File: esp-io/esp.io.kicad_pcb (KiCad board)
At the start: 2 copper layers, 91.9 x 86 mm, 76 parts, among them P1 CONN_2, P2 CONN_01X02, P3 CONN_01X02, P4 CONN_01X02, P5 CONN_01X02, Q1 NPN, Q2 NPN, Q3 NPN, Q4 NPN, Q5 NPN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

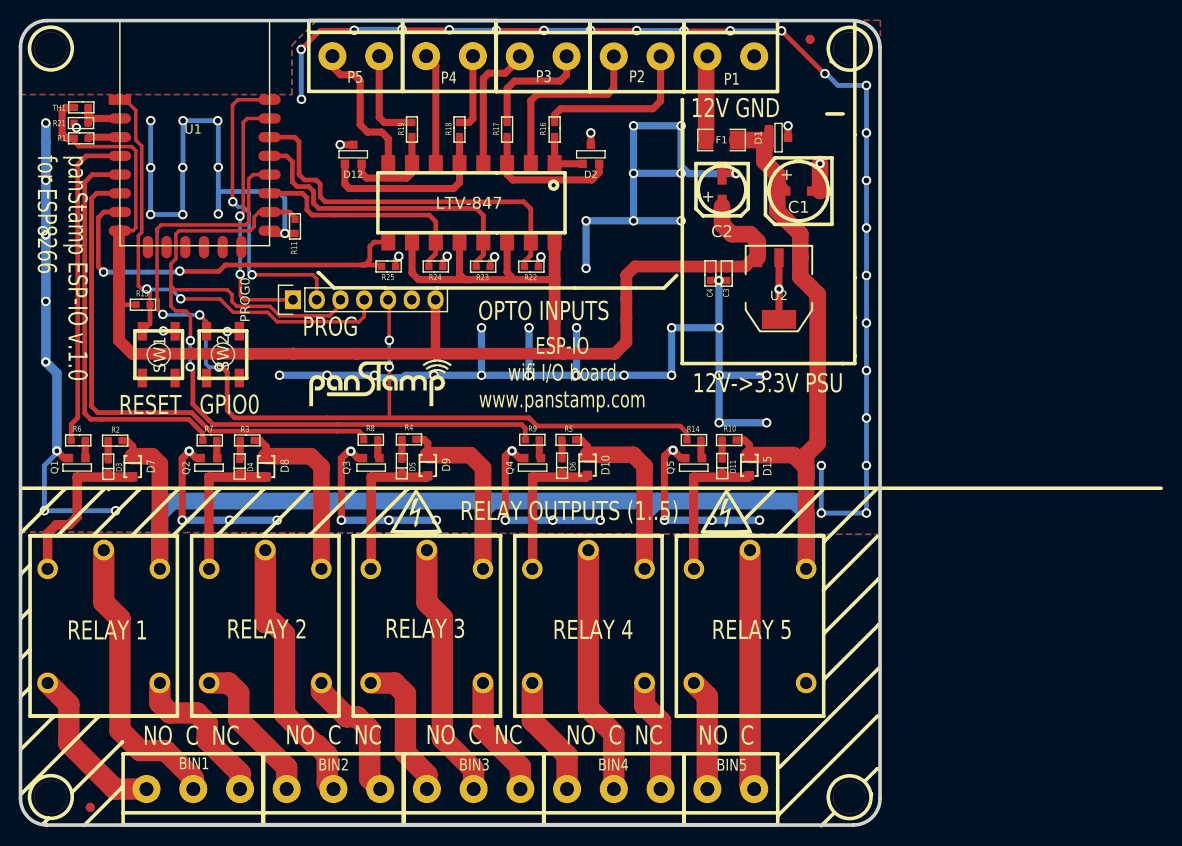
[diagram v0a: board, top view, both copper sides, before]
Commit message: fifth relay removed
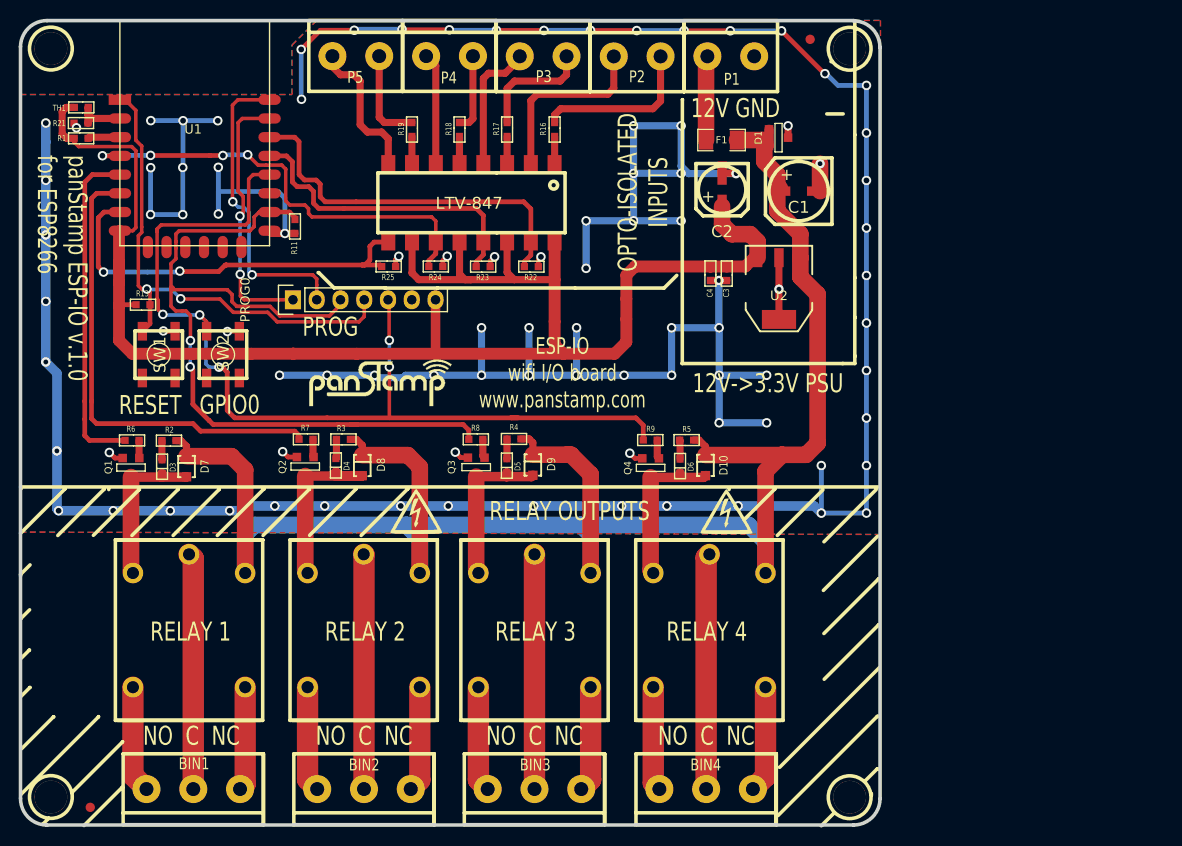
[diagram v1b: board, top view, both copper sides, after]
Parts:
- removed BIN5: CONN_2, myconnectors:terminal_block_5mm_2P
- removed D11: LED, SM0603S_POL
- removed D12, D2: D_Schottky_x2_ACom_KKA, mysmd:SOT23
- removed D15: DIODE, SOD323
- removed Q5: NPN, SOT23EBC
- removed R10: 1k5, SM0603S
- removed R14: 2k2, SM0603S
- removed U7: SONGLE_RELAY_10A, SONGLE_RELAY_10A
- moved U6 12.9 mm to (209.0, 108.0)
- moved D6 12.6 mm to (205.9, 90.5)
- moved D10 12.6 mm to (208.6, 90.4)
- moved Q4 12.6 mm to (202.7, 90.7)
- moved R5 12.6 mm to (206.6, 87.7)
- moved R9 12.6 mm to (202.7, 87.7)
- moved U5 11.5 mm to (190.3, 108.0)
- moved D5 11.2 mm to (187.4, 90.4)
- moved R4 11.2 mm to (188.1, 87.6)
- moved D9 11.2 mm to (190.1, 90.4)
- moved Q3 11.2 mm to (184.1, 90.6)
- moved R8 11.2 mm to (184.0, 87.6)
- moved U4 10.5 mm to (172.1, 108.0)
- moved Q2 10.3 mm to (165.8, 90.5)
- moved R3 10.3 mm to (169.9, 87.6)
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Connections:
- PROG0 pad 3: BINOUT3 -> BINOUT2
- PROG0 pad 5: BINOUT4 -> BINOUT3
- R11 pad 2: BINOUT3 -> BINOUT2
- R24 pad 2: /GPIO2 -> /GPIO16
- SW2 pad 2: BINOUT4 -> BINOUT3
- U1 pad 16: BINOUT3 -> BINOUT2
- U1 pad 18: BINOUT4 -> BINOUT3
- U1 pad 4: BINOUT0 -> /GPIO16
- U1 pad 5: BINOUT1 -> BINOUT0
- U1 pad 6: BINOUT2 -> BINOUT1
- U8 pad 11: /GPIO2 -> /GPIO16
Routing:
- net GND: track 348.3 -> 189.5 mm, vias 74 -> 45
- net (no net): track 125.5 -> 275.5 mm, vias 25 -> 50
- net BINOUT4: track 108.4 -> 0.00 mm, vias 5 -> 0
- net /GPIO16: track 0.00 -> 48.0 mm, vias 0 -> 4
- net +12C: track 249.9 -> 208.7 mm
- net BINOUT2: track 56.3 -> 88.4 mm, vias 0 -> 2
- net Net-(BIN5-Pad2): track 25.7 -> 0.00 mm
- net /GPIO2: track 24.9 -> 0.00 mm
- net Net-(R18-Pad1): track 19.8 -> 2.88 mm
- net Net-(D11-Pad2): track 16.3 -> 0.00 mm
- net Net-(R17-Pad1): track 15.4 -> 2.88 mm
- net Net-(BIN5-Pad1): track 11.9 -> 0.00 mm
- net BINOUT3: track 93.9 -> 104.9 mm, vias 2 -> 5
- net Net-(R19-Pad1): track 12.1 -> 4.29 mm
- net BINOUT1: track 43.1 -> 50.1 mm
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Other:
- board text added: "OPTO-ISOLATED INPUTS"
- board text added: "RELAY OUTPUTS"
- board text removed: "NO C"
- board text removed: "OPTO INPUTS"
- board text removed: "RELAY 5"
- board text removed: "RELAY OUTPUTS (1..5)"
